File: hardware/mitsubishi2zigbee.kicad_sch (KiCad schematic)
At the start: 10 parts, among them J1 Conn_01x05, Q1 BSS138, Q2 BSS138

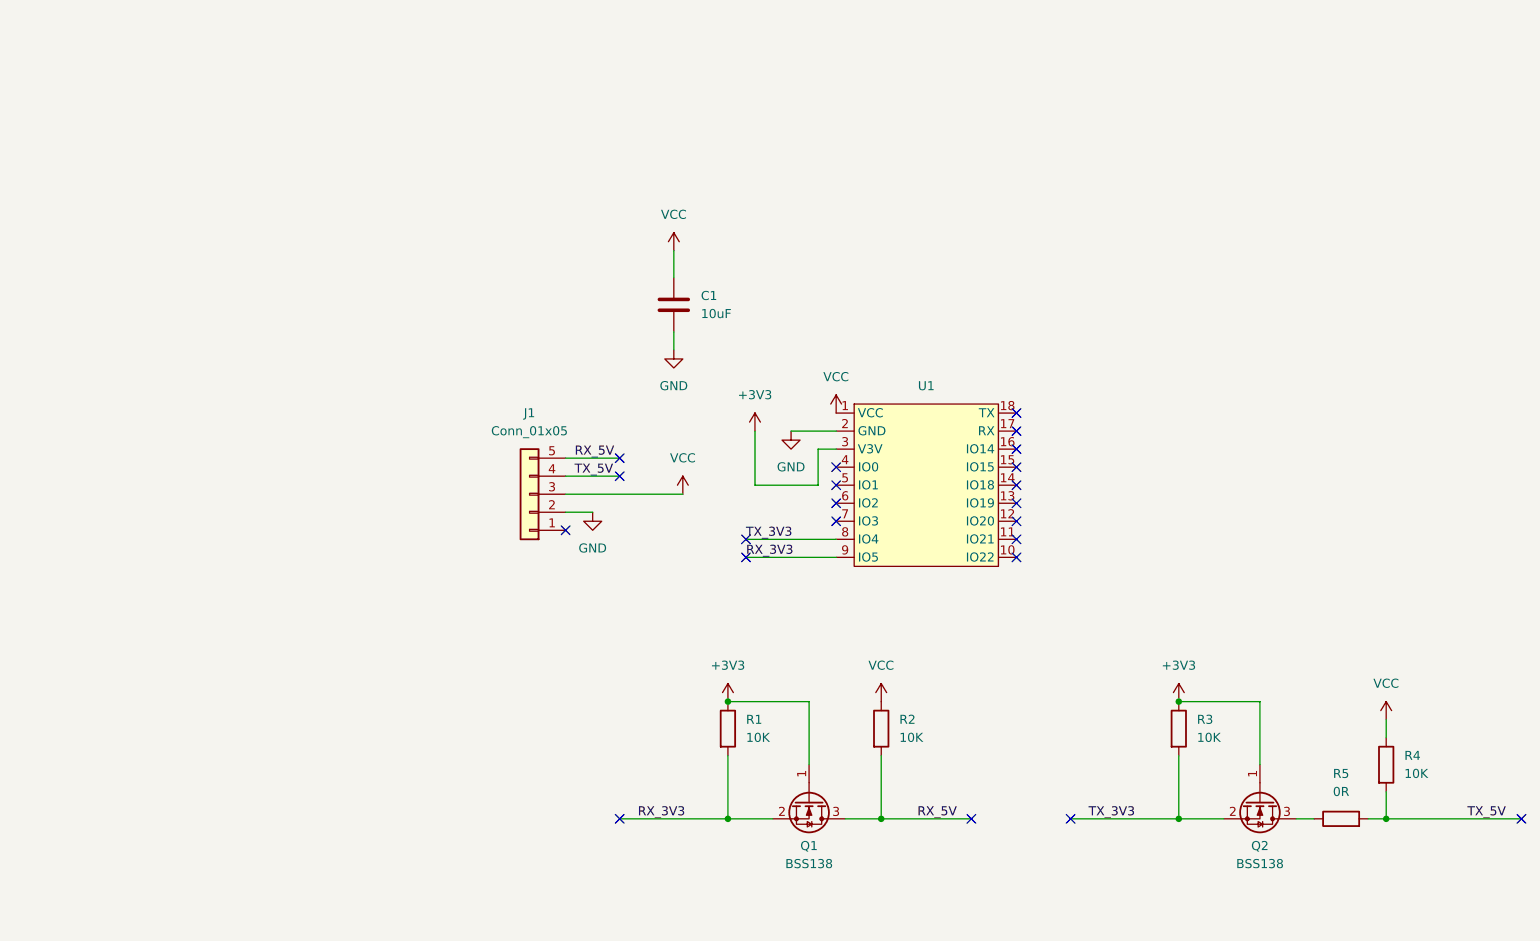
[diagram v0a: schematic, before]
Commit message: Update KiCad hardware schematic layout and component labels.
Reorganize schematic into functional sections and rename CN105/ESP32-C6 values for clarity.
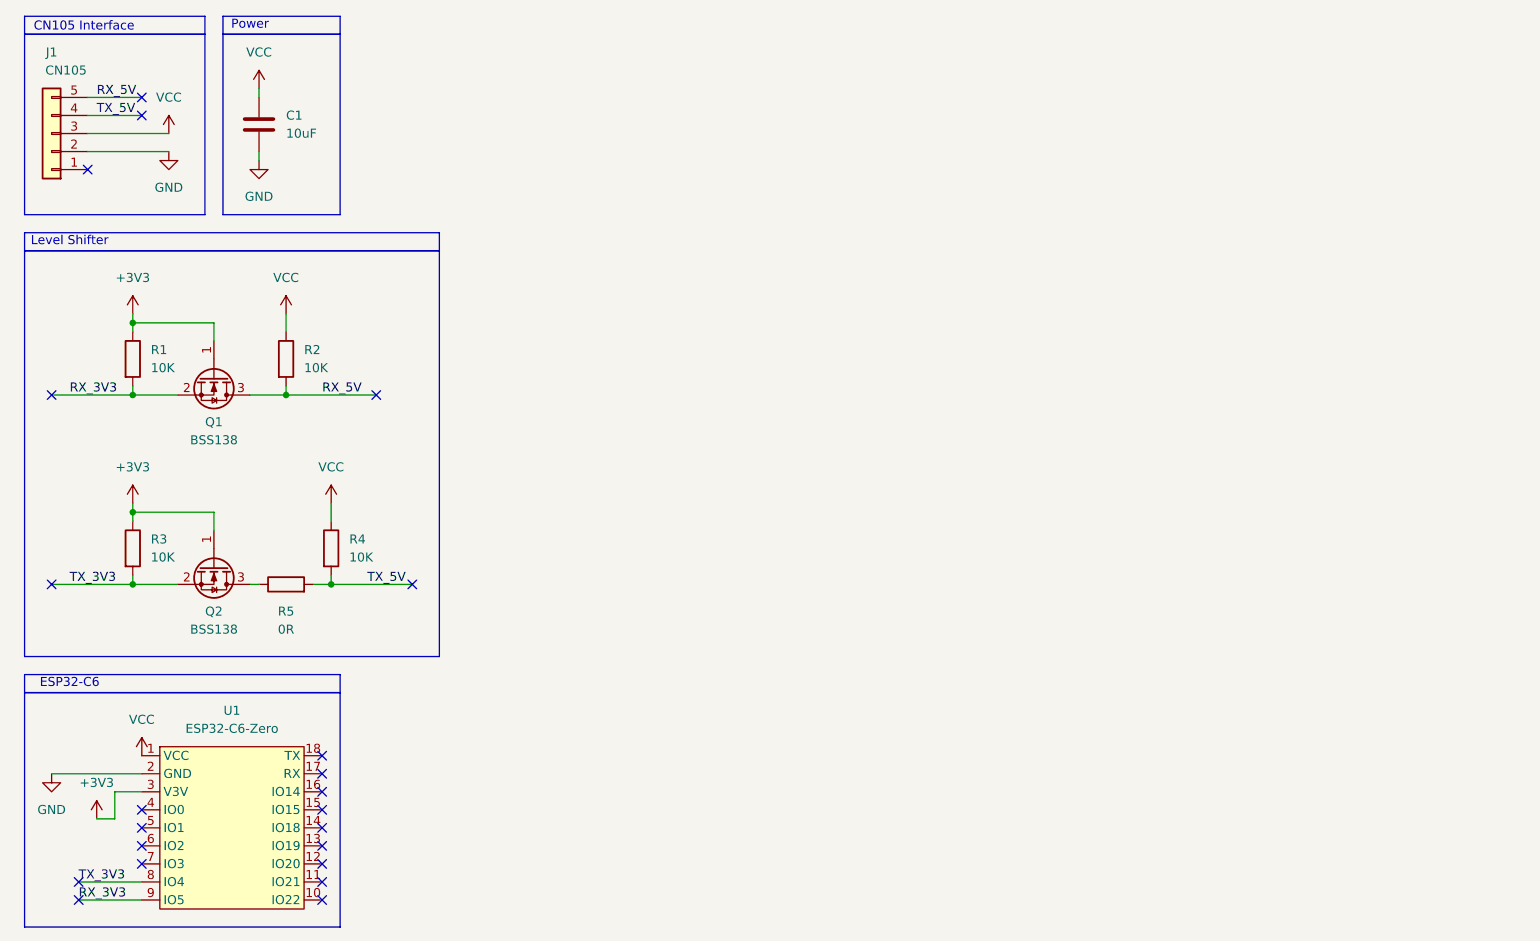
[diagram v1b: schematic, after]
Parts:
- J1: value Conn_01x05 -> CN105
- U1: value (none) -> ESP32-C6-Zero
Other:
- note added: "CN105 Interface"
- note added: "ESP32-C6"
- note added: "Level Shifter"
- note added: "Power"
- moved on the sheet: C1, J1, Q1, Q2, R1, R2, R3, R4, R5, U1
